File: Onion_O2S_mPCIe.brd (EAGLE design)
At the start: 30 x 50.9 mm, 7 parts, among them J1 693071020811, U1 ONION_OMEGA2S

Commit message: continued layout
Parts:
- added LED1: (no value), led:CHIPLED_0603
- added R1: (no value), rcl:R0603
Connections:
- new net N$1: LED1.C, R1.2
- net !WLED: now also R1.1
- net +3V3: now also LED1.A
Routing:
- net UART1_RX: track 0.00 -> 48.2 mm, vias 0 -> 2
- net UART1_TX: track 0.00 -> 46.8 mm, vias 0 -> 1
- net !WLED: track 0.00 -> 28.2 mm
- net N$1: track 0.00 -> 22.7 mm
- net USB_D_N: track 23.4 -> 25.4 mm, vias 0 -> 1
- net USB_D_P: track 23.9 -> 25.9 mm, vias 0 -> 1
- net ETH0_TXO_N: track 45.3 -> 46.8 mm
- net ETH0_TXO_P: track 45.8 -> 47.3 mm
- net +3V3: track 10.2 -> 10.9 mm, vias 6 -> 7
- net ETH0_RXI_P: track 44.1 -> 43.5 mm
- net GND: vias 24 -> 23
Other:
- board text added: "Onion Omega2S+ mPCIe"

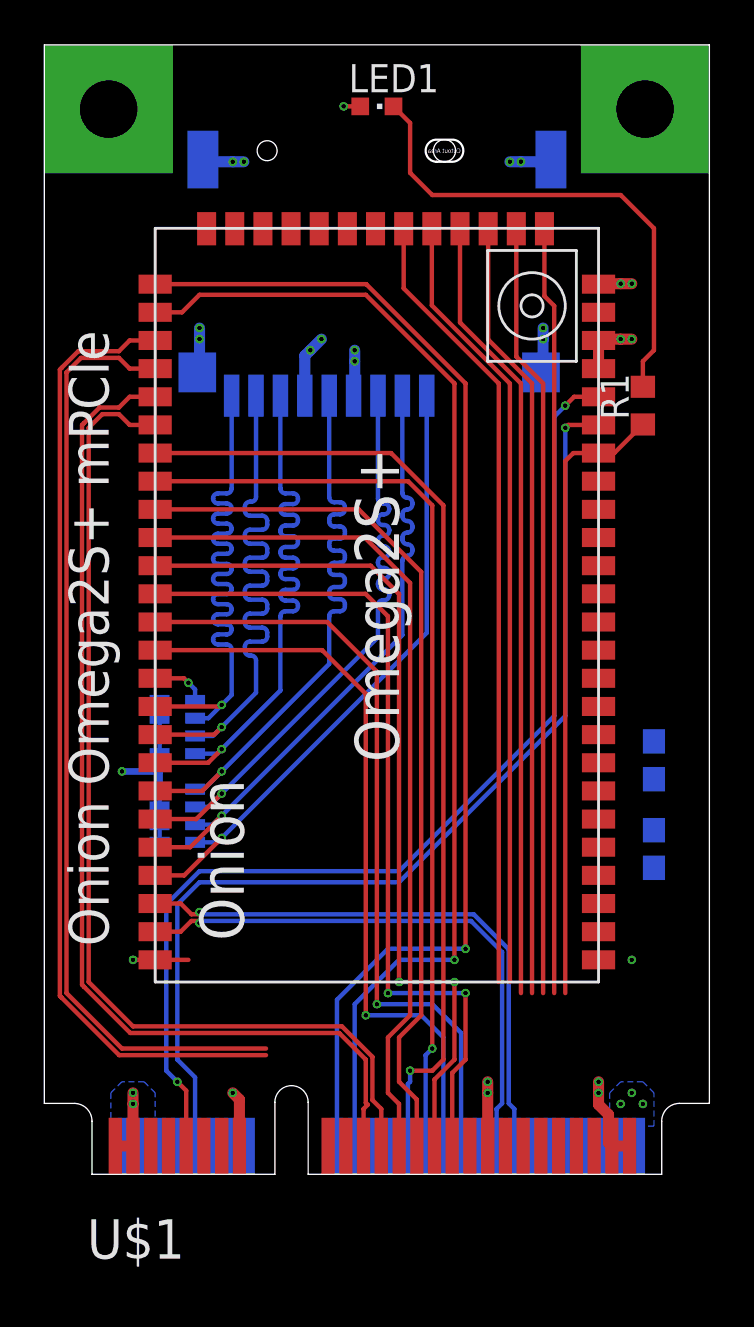
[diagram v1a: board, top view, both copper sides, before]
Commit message: * Completely changed pinout * Started Eval Board
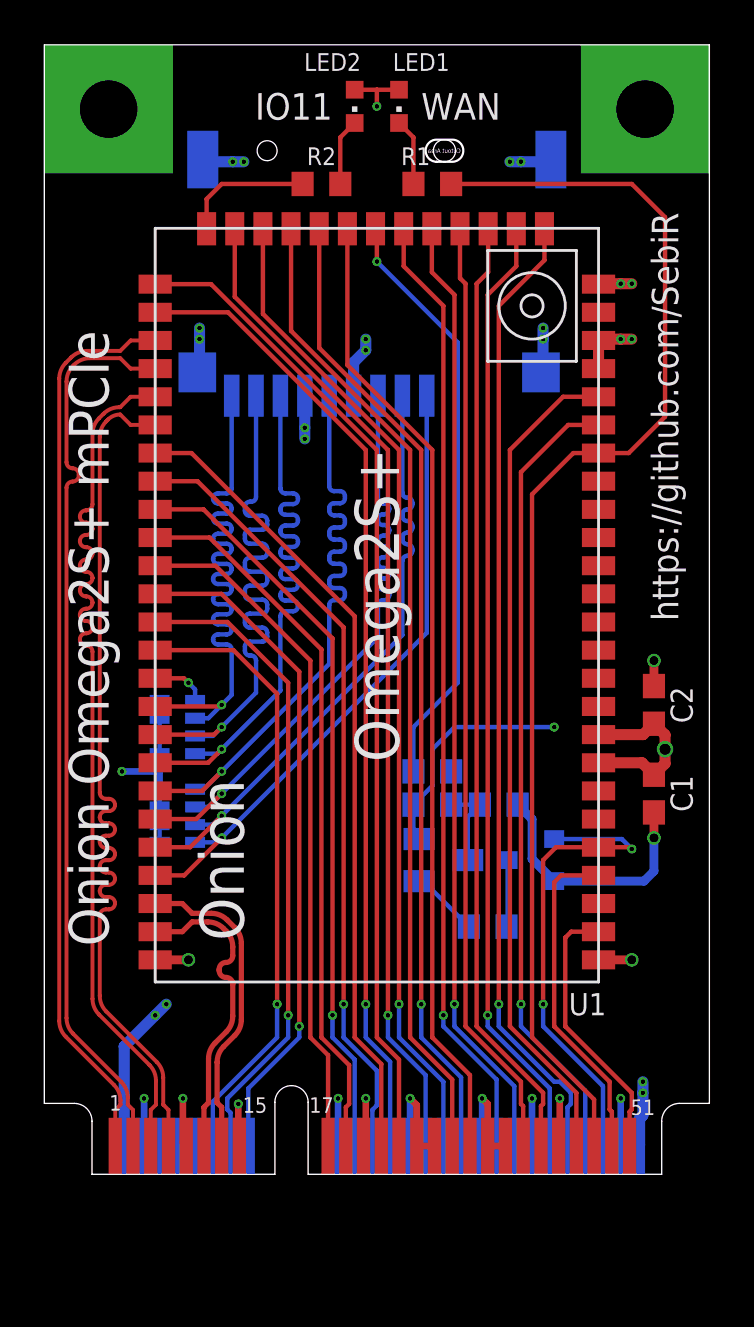
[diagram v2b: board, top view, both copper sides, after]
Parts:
- added LED2: (no value), led:CHIPLED_0603
- added Q2: 5.8A/30V/35mΩ, SparkFun-DiscreteSemi:SOT23-3
- added Q3: BC807-16SMD, transistor-pnp:SOT23-BEC
- added R2: (no value), rcl:R0603
- added R3, R9: 10k, rcl:R0603
- added R4, R5: 0R, rcl:R0603
- moved R1 13.8 mm to (17.5, 41.5), turned to 180 degrees
- moved C1 2.50 mm to (27.5, 14.0), flipped to the top
- moved C2 2.50 mm to (27.5, 18.0), flipped to the top
- moved LED1 1.00 mm to (16.0, 45.0), turned to 180 degrees
- renumbered U$1 to EDGECON1
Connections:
- removed net ETH0_RXI_P: EDGECON1.24, U1.41
- removed net ETH0_TXO_P: EDGECON1.21, U1.43
- removed net USB_D_P: EDGECON1.38, U1.61
- new net !HW_RST: EDGECON1.48, Q2.1, U1.5
- new net !PERST: EDGECON1.51, U1.2
- new net ETH0_RXI_+: EDGECON1.1, U1.41
- new net ETH0_TXO_+: EDGECON1.5, U1.43
- new net LED: R2.1, U1.38
- new net N$2: Q3.B, R9.2
- new net N$3: Q2.3, R9.1
- new net N$4: Q3.C, R3.2, R4.1, R5.2
- new net N$7: LED2.C, R2.2
- new net SPI_CLK: EDGECON1.32, U1.34
- new net SPI_CS0: EDGECON1.28, U1.37
- new net SPI_CS1: EDGECON1.33, U1.33
- new net SPI_MISO: EDGECON1.31, U1.35
- new net SPI_MOSI: EDGECON1.30, U1.36
- new net SW_RST: EDGECON1.49, U1.4
- new net USB_D_+: EDGECON1.13, U1.61
- new net VDD_FLASH: R5.1, U1.32
- net !WLED: now also EDGECON1.47; no longer EDGECON1.44
- net +3V3: now also LED2.A, Q3.E, R4.2; no longer EDGECON1.4, EDGECON1.50
- net ETH0_RXI_N: now also EDGECON1.3; no longer EDGECON1.22
- net ETH0_TXO_N: now also EDGECON1.7; no longer EDGECON1.23
- net GND: now also EDGECON1.18, EDGECON1.21, EDGECON1.26, EDGECON1.27, EDGECON1.29, EDGECON1.34, EDGECON1.37, EDGECON1.4, EDGECON1.40, EDGECON1.43, EDGECON1.50, EDGECON1.9, EDGECON1.M1, EDGECON1.M2, Q2.2, R3.1; no longer EDGECON1.1, EDGECON1.3, EDGECON1.49, EDGECON1.51
- net GPIO_14: now also EDGECON1.23; no longer EDGECON1.26
- net GPIO_15: now also EDGECON1.22; no longer EDGECON1.28
- net GPIO_16: now also EDGECON1.20; no longer EDGECON1.27
- net GPIO_17: now also EDGECON1.19; no longer EDGECON1.25
- net GPIO_18: now also EDGECON1.17; no longer EDGECON1.29
- net GPIO_19: now also EDGECON1.16; no longer EDGECON1.31
- net GPIO_20: now also EDGECON1.14; no longer EDGECON1.32
- net GPIO_21: now also EDGECON1.12; no longer EDGECON1.30
- net I2C_SCK: now also EDGECON1.38; no longer EDGECON1.47
- net I2C_SDA: now also EDGECON1.36; no longer EDGECON1.48
- net I2S_SDI: now also EDGECON1.44; no longer EDGECON1.41
- net I2S_SDO: now also EDGECON1.42; no longer EDGECON1.43
- net I2S_WS: now also EDGECON1.41; no longer EDGECON1.40
- net UART0_RX: now also EDGECON1.24; no longer EDGECON1.20
- net UART0_TX: now also EDGECON1.25; no longer EDGECON1.18
- net UART1_RX: now also EDGECON1.45; no longer EDGECON1.9
- net UART1_TX: now also EDGECON1.46; no longer EDGECON1.10
- net USB_D_N: now also EDGECON1.11; no longer EDGECON1.36
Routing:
- net ETH0_TXO_P: track 47.3 -> 0.00 mm
- net SPI_CS0: track 0.00 -> 44.9 mm, vias 0 -> 1
- net SPI_MOSI: track 0.00 -> 44.8 mm, vias 0 -> 1
- net SPI_MISO: track 0.00 -> 44.4 mm
- net SPI_CLK: track 0.00 -> 44.0 mm, vias 0 -> 1
- net SPI_CS1: track 0.00 -> 43.7 mm
- net ETH0_RXI_P: track 43.5 -> 0.00 mm
- net ETH0_RXI_+: track 0.00 -> 40.9 mm
- net ETH0_TXO_+: track 0.00 -> 39.9 mm
- net +3V3: track 10.9 -> 42.4 mm, vias 7 -> 10
- net !WLED: track 28.2 -> 57.3 mm
- net GND: track 30.1 -> 57.5 mm, vias 23 -> 28
- net VDD_FLASH: track 0.00 -> 26.8 mm, vias 0 -> 1
- net USB_D_P: track 25.9 -> 0.00 mm, vias 1 -> 0
- net !HW_RST: track 0.00 -> 22.0 mm, vias 0 -> 2
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- removed copper zone on layer 16, net +3V3
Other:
- board text added: "1"
- board text added: "15"
- board text added: "16"
- board text added: "17"
- board text added: "18"
- board text added: "2"
- board text added: "51"
- board text added: "52"
- board text added: "IO11"
- board text added: "WAN"
- board text added: "https://github.com/SebiR"

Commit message: - small changes to the sikscreen of the module - continued design of Eval Board
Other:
- board text added: "made for"
